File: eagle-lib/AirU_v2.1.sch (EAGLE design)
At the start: 85 parts, among them J1 DNP, J2 4p-2.54, Q1 BSS138W-7-F, Q2 MMBT3904LT1G, Q3 MMBT3904LT1G, Q5 NCE3407A, U1 HDC1080DMBT, U2 CH340T-SSOP20, U3 CJT1117-3.3-SOT223, U4 MAX2659-DFN6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

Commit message: updated to v2.1
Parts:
- removed J1: DNP, Seeed-Connector:DIP-BLACK-MALE-HEADER(6P-2.54)
- removed J2: 4p-2.54, Seeed-Connector:DIP-BLACK-MALE-HEADER-VERT(4P-2.54)
- removed R35: 220R, Seeed-Resistor:SMD-RES-220R-5%-1/10W(0603)
- added 3.3V, 5.0V, GND: TPTP20SQ, testpad:TPTP20SQ
- added R25: 220R, Seeed-Resistor:SMD-RES-220R-5%-1/10W(0603)
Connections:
- net N$15 renamed V_BCKP
- removed net GPIO11: J1.5, U7.CMD
- removed net GPIO6: J1.4, U7.CLK
- removed net GPIO7: J1.3, U7.SD0
- removed net GPIO8: J1.2, U7.SD1
- removed net N$17: R38.1, U5.TXD1
- removed net N$31: R35.2, U7.SD3
- removed net STANDBY: U5.STANDBY, U7.IO22
- removed net TIMER: U5.TIMER, U7.IO23
- new net ESP-RXD: R38.2, U7.IO23
- new net ESP-TXD: R25.2, U7.IO22
- net 1PPS: now also U7.IO39/SEN_VN/A1_3; no longer U7.I34/A1_6
- net 3.3V: now also 3.3V.TP
- net 5.0V: now also 5.0V.TP
- net GND: now also GND.TP; no longer J1.1, J1.6, J2.P$1, J2.P$2, J2.P$3, J2.P$4
- net MICS_PREHEAT_NOX: now also U7.IO32/A1_4/X32P; no longer U7.I35/A1_7
- net MICS_PWR: now also U7.IO33/A1_5/X32N; no longer U7.IO32/A1_4/X32P
- net RESET: now also Q3.C; no longer Q3.E
- net RTS: now also Q3.E; no longer Q3.C
- net U1RXD: now also R25.1, U5.RXD1; no longer R38.2, U7.SD2
- net U1TXD: now also R38.1, U5.TXD1; no longer R35.1, U5.RXD1
- net VOX_RAWB: now also U7.I34/A1_6; no longer U7.IO33/A1_5/X32N
- net VRED_RAWB: now also U7.I35/A1_7; no longer U7.IO25/DAC1/A2_8
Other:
- note added: "AirU v2.1 w/ ESP32-WROOM32"
- note added: "GPIOs 6-11 are ESP32 flashing pins. Dont use them."
- note added: "November 12, 2018"
- note removed: "AirU v2.0 w/ ESP32-WROOM32"
- note removed: "PIN HEADERS"
- note removed: "Pin headers for foam to hold board in housing."
- note removed: "September 21, 2018"
- note removed: "Septemter 21, 2018"
- moved on the sheet: C2, C23, C27, C28, Q3, R10, R22, R37, U1, U6, U8

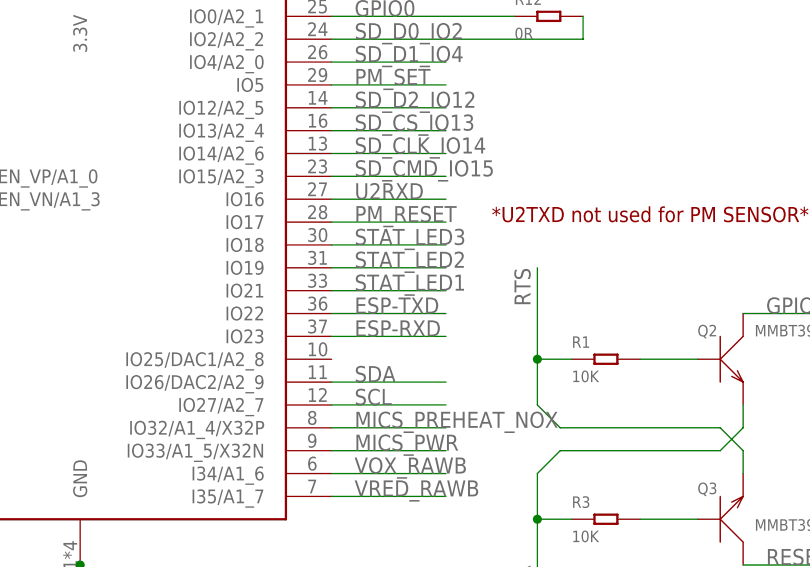
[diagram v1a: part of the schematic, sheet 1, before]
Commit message: updated board
changed PM_RESET to an RTC GPIO (previously unpopulated), and changed the logo/revision info
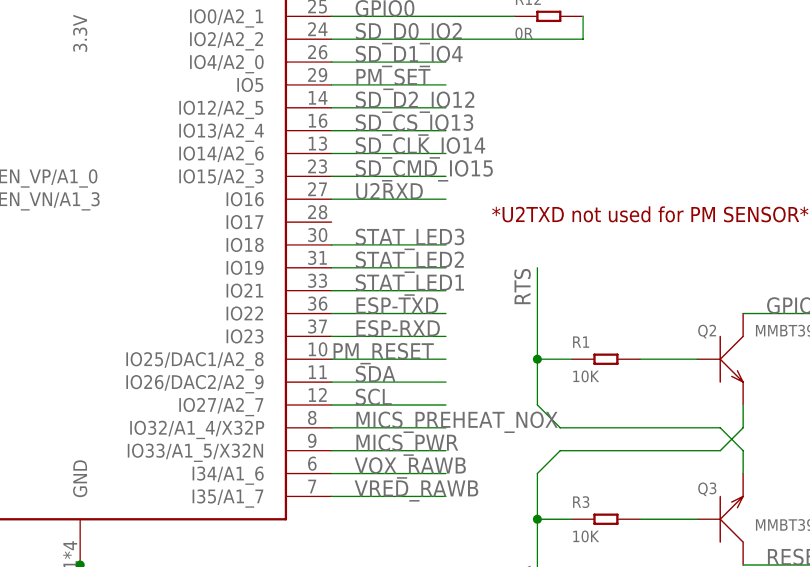
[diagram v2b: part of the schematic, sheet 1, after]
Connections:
- net PM_RESET: now also U7.IO25/DAC1/A2_8; no longer U7.IO17
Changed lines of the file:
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@@
 <?xml version="1.0" encoding="utf-8"?>
 <!DOCTYPE eagle SYSTEM "eagle.dtd">
-<eagle version="9.2.2">
+<eagle version="9.6.2">
 <drawing>
 <settings>
@@
 <net name="PM_RESET" class="0">
 <segment>
-<pinref part="U7" gate="G$1" pin="IO17"/>
-<wire x1="78.74" y1="93.98" x2="91.44" y2="93.98" width="0.1524" layer="91"/>
-<label x="81.28" y="93.98" size="1.778" layer="95"/>
-</segment>
-</net>
+<pinref part="U7" gate="G$1" pin="IO25/DAC1/A2_8"/>
+<wire x1="78.74" y1="78.74" x2="91.44" y2="78.74" width="0.1524" layer="91"/>
+<label x="78.74" y="78.74" size="1.778" layer="95"/>
+</segment>
+</net>
